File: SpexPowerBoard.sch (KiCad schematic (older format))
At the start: 12 parts

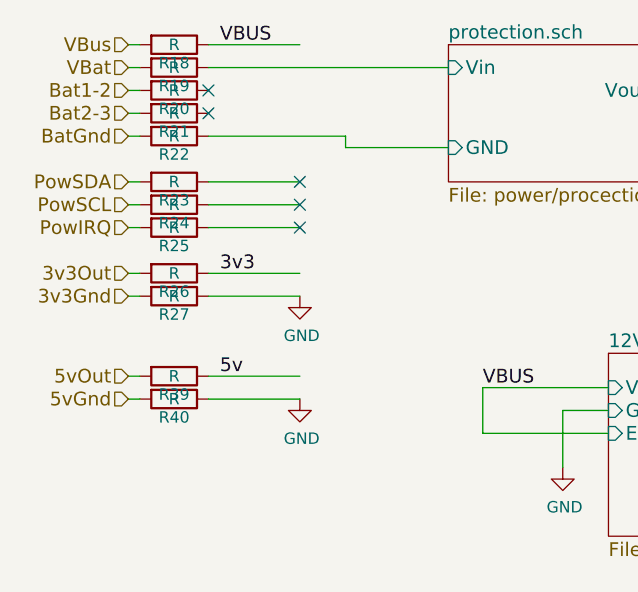
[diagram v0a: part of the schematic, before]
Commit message: Added powerz
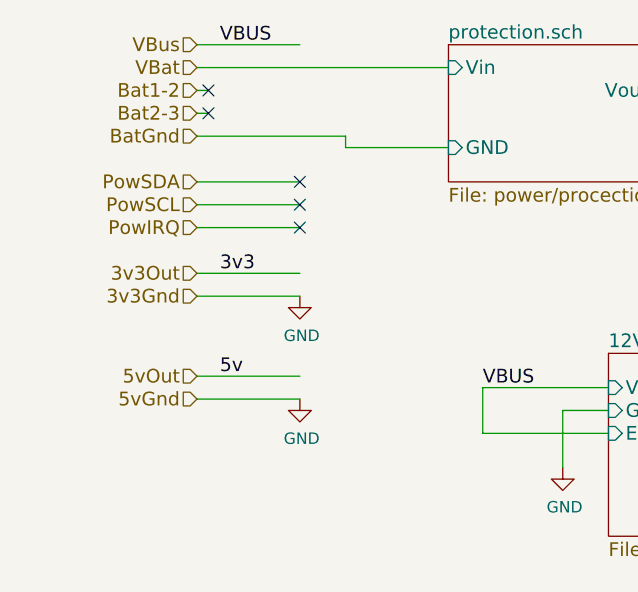
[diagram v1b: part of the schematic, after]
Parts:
- removed R18, R19, R20, R21, R22, R23, R24, R25, R26, R27, R39, R40: R, Resistors_SMD:R_0603, symbol R
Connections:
- wire segments 37 -> 27
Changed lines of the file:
@@
 Comment4 ""
 $EndDescr
-Text HLabel 1950 800  0    60   Input ~ 0
+Text HLabel 2250 800  0    60   Input ~ 0
 VBus
-Text HLabel 1950 900  0    60   Input ~ 0
+Text HLabel 2250 900  0    60   Input ~ 0
 VBat
-Text HLabel 1950 1000 0    60   Input ~ 0
+Text HLabel 2250 1000 0    60   Input ~ 0
 Bat1-2
-Text HLabel 1950 1100 0    60   Input ~ 0
+Text HLabel 2250 1100 0    60   Input ~ 0
 Bat2-3
-Text HLabel 1950 1200 0    60   Input ~ 0
+Text HLabel 2250 1200 0    60   Input ~ 0
 BatGnd
-Text HLabel 1950 1400 0    60   Input ~ 0
+Text HLabel 2250 1400 0    60   Input ~ 0
 PowSDA
-Text HLabel 1950 1500 0    60   Input ~ 0
+Text HLabel 2250 1500 0    60   Input ~ 0
 PowSCL
-Text HLabel 1950 1600 0    60   Input ~ 0
+Text HLabel 2250 1600 0    60   Input ~ 0
 PowIRQ
-Text HLabel 1950 1800 0    60   Input ~ 0
+Text HLabel 2250 1800 0    60   Input ~ 0
 3v3Out
-Text HLabel 1950 1900 0    60   Input ~ 0
+Text HLabel 2250 1900 0    60   Input ~ 0
 3v3Gnd
-$Comp
-L R R18
-U 1 1 56DE6203
-P 2150 800
-F 0 "R18" V 2230 800 50  0000 C CNN
-F 1 "R" V 2150 800 50  0000 C CNN
-F 2 "Resistors_SMD:R_0603" V 2080 800 50  0001 C CNN
-F 3 "" H 2150 800 50  0000 C CNN
-	1    2150 800
-	0    1    1    0
-$EndComp
-$Comp
-L R R19
-U 1 1 56DE621B
-P 2150 900
-F 0 "R19" V 2230 900 50  0000 C CNN
-F 1 "R" V 2150 900 50  0000 C CNN
-F 2 "Resistors_SMD:R_0603" V 2080 900 50  0001 C CNN
-F 3 "" H 2150 900 50  0000 C CNN
-	1    2150 900
-	0    1    1    0
-$EndComp
-$Comp
-L R R20
-U 1 1 56DE6236
-P 2150 1000
-F 0 "R20" V 2230 1000 50  0000 C CNN
-F 1 "R" V 2150 1000 50  0000 C CNN
-F 2 "Resistors_SMD:R_0603" V 2080 1000 50  0001 C CNN
-F 3 "" H 2150 1000 50  0000 C CNN
-	1    2150 1000
-	0    1    1    0
-$EndComp
-$Comp
-L R R21
-U 1 1 56DE6251
-P 2150 1100
-F 0 "R21" V 2230 1100 50  0000 C CNN
-F 1 "R" V 2150 1100 50  0000 C CNN
-F 2 "Resistors_SMD:R_0603" V 2080 1100 50  0001 C CNN
-F 3 "" H 2150 1100 50  0000 C CNN
-	1    2150 1100
-	0    1    1    0
-$EndComp
-$Comp
-L R R22
-U 1 1 56DE626E
-P 2150 1200
-F 0 "R22" V 2230 1200 50  0000 C CNN
-F 1 "R" V 2150 1200 50  0000 C CNN
-F 2 "Resistors_SMD:R_0603" V 2080 1200 50  0001 C CNN
-F 3 "" H 2150 1200 50  0000 C CNN
-	1    2150 1200
-	0    1    1    0
-$EndComp
-$Comp
-L R R23
-U 1 1 56DE6291
-P 2150 1400
-F 0 "R23" V 2230 1400 50  0000 C CNN
-F 1 "R" V 2150 1400 50  0000 C CNN
-F 2 "Resistors_SMD:R_0603" V 2080 1400 50  0001 C CNN
-F 3 "" H 2150 1400 50  0000 C CNN
-	1    2150 1400
-	0    1    1    0
-$EndComp
-$Comp
-L R R24
-U 1 1 56DE62B4
-P 2150 1500
-F 0 "R24" V 2230 1500 50  0000 C CNN
-F 1 "R" V 2150 1500 50  0000 C CNN
-F 2 "Resistors_SMD:R_0603" V 2080 1500 50  0001 C CNN
-F 3 "" H 2150 1500 50  0000 C CNN
-	1    2150 1500
-	0    1    1    0
-$EndComp
-$Comp
-L R R25
-U 1 1 56DE62DB
-P 2150 1600
-F 0 "R25" V 2230 1600 50  0000 C CNN
-F 1 "R" V 2150 1600 50  0000 C CNN
-F 2 "Resistors_SMD:R_0603" V 2080 1600 50  0001 C CNN
-F 3 "" H 2150 1600 50  0000 C CNN
-	1    2150 1600
-	0    1    1    0
-$EndComp
-$Comp
-L R R26
-U 1 1 56DE6304
-P 2150 1800
-F 0 "R26" V 2230 1800 50  0000 C CNN
-F 1 "R" V 2150 1800 50  0000 C CNN
-F 2 "Resistors_SMD:R_0603" V 2080 1800 50  0001 C CNN
-F 3 "" H 2150 1800 50  0000 C CNN
-	1    2150 1800
-	0    1    1    0
-$EndComp
-$Comp
-L R R27
-U 1 1 56DE632D
-P 2150 1900
-F 0 "R27" V 2230 1900 50  0000 C CNN
-F 1 "R" V 2150 1900 50  0000 C CNN
-F 2 "Resistors_SMD:R_0603" V 2080 1900 50  0001 C CNN
-F 3 "" H 2150 1900 50  0000 C CNN
-	1    2150 1900
-	0    1    1    0
-$EndComp
 $Sheet
 S 4050 2150 800  800
@@
 VBUS
 $Comp
-L GND #PWR057
+L GND #PWR058
 U 1 1 56FE58A8
 P 3850 2650
-F 0 "#PWR057" H 3850 2400 50  0001 C CNN
+F 0 "#PWR058" H 3850 2400 50  0001 C CNN
 F 1 "GND" H 3858 2477 50  0000 C CNN
 F 2 "" H 3850 2650 50  0000 C CNN
@@
 $EndComp
 Wire Wire Line
-	1950 800  2000 800
+	2250 800  2700 800
 Wire Wire Line
-	1950 900  2000 900
+	2250 900  3350 900
 Wire Wire Line
-	1950 1000 2000 1000
+	2250 1000 2300 1000
 Wire Wire Line
-	1950 1100 2000 1100
+	2250 1100 2300 1100
 Wire Wire Line
-	1950 1200 2000 1200
+	2250 1200 2900 1200
 Wire Wire Line
-	1950 1400 2000 1400
+	2250 1400 2700 1400
 Wire Wire Line
-	1950 1500 2000 1500
+	2250 1500 2700 1500
 Wire Wire Line
-	1950 1600 2000 1600
+	2250 1600 2700 1600
 Wire Wire Line
-	1950 1800 2000 1800
+	2250 1800 2700 1800
 Wire Wire Line
-	1950 1900 2000 1900
-Wire Wire Line
-	2300 900  3350 900
+	2250 1900 2700 1900
 Wire Wire Line
 	2900 1250 3350 1250
 Wire Wire Line
-	2900 1250 2900 1200
-Wire Wire Line
-	2900 1200 2300 1200
+	2900 1200 2900 1250
 Wire Wire Line
 	4300 1000 4550 1000
@@
 VBUS
 $Comp
-L GND #PWR058
+L GND #PWR059
 U 1 1 56FE6215
 P 3850 4250
-F 0 "#PWR058" H 3850 4000 50  0001 C CNN
+F 0 "#PWR059" H 3850 4000 50  0001 C CNN
 F 1 "GND" H 3858 4077 50  0000 C CNN
 F 2 "" H 3850 4250 50  0000 C CNN
@@
 Text Label 4900 3950 0    60   ~ 0
 5v
-Wire Wire Line
-	2300 1400 2700 1400
-Wire Wire Line
-	2300 1500 2700 1500
-Wire Wire Line
-	2300 1600 2700 1600
-Wire Wire Line
-	2300 1800 2700 1800
-Wire Wire Line
-	2300 1900 2700 1900
 Text Label 2350 1800 0    60   ~ 0
 3v3
 $Comp
-L GND #PWR059
+L GND #PWR060
 U 1 1 56FE74FE
 P 2700 1900
-F 0 "#PWR059" H 2700 1650 50  0001 C CNN
+F 0 "#PWR060" H 2700 1650 50  0001 C CNN
 F 1 "GND" H 2708 1727 50  0000 C CNN
 F 2 "" H 2700 1900 50  0000 C CNN
@@
 NoConn ~ 2300 1000
 NoConn ~ 2300 1100
-Wire Wire Line
-	2300 800  2700 800
 Text Label 2350 800  0    60   ~ 0
 VBUS
-Text HLabel 1950 2250 0    60   Input ~ 0
+Text HLabel 2250 2250 0    60   Input ~ 0
 5vOut
-Text HLabel 1950 2350 0    60   Input ~ 0
+Text HLabel 2250 2350 0    60   Input ~ 0
 5vGnd
-$Comp
-L R R39
-U 1 1 56FE7B52
-P 2150 2250
-F 0 "R39" V 2230 2250 50  0000 C CNN
-F 1 "R" V 2150 2250 50  0000 C CNN
-F 2 "Resistors_SMD:R_0603" V 2080 2250 50  0001 C CNN
-F 3 "" H 2150 2250 50  0000 C CNN
-	1    2150 2250
-	0    1    1    0
-$EndComp
-$Comp
-L R R40
-U 1 1 56FE7B58
-P 2150 2350
-F 0 "R40" V 2230 2350 50  0000 C CNN
-F 1 "R" V 2150 2350 50  0000 C CNN
-F 2 "Resistors_SMD:R_0603" V 2080 2350 50  0001 C CNN
-F 3 "" H 2150 2350 50  0000 C CNN
-	1    2150 2350
-	0    1    1    0
-$EndComp
 Wire Wire Line
-	1950 2250 2000 2250
+	2250 2250 2700 2250
 Wire Wire Line
-	1950 2350 2000 2350
-Wire Wire Line
-	2300 2250 2700 2250
-Wire Wire Line
-	2300 2350 2700 2350
+	2250 2350 2700 2350
 Text Label 2350 2250 0    60   ~ 0
 5v
 $Comp
-L GND #PWR060
+L GND #PWR061
 U 1 1 56FE7B63
 P 2700 2350
-F 0 "#PWR060" H 2700 2100 50  0001 C CNN
+F 0 "#PWR061" H 2700 2100 50  0001 C CNN
 F 1 "GND" H 2708 2177 50  0000 C CNN
 F 2 "" H 2700 2350 50  0000 C CNN

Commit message: completed first revision of the board.
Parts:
- added P13: CONN_01X02, SPEX_Parts:ultraFitCONN_2, symbol CONN_01X02
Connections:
- wire segments 27 -> 30
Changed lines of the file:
@@
 3v3Gnd
 $Sheet
-S 4050 2150 800  800
+S 5600 800  800  800
 U 56FE3A4E
 F0 "12Vto3v3.sch" 60
 F1 "power/12Vto3v3.sch" 60
-F2 "Vin" I L 4050 2300 60
-F3 "Gnd" I L 4050 2400 60
-F4 "En" I L 4050 2500 60
-F5 "Vout" I R 4850 2300 60
+F2 "Vin" I L 5600 950 60
+F3 "Gnd" I L 5600 1050 60
+F4 "En" I L 5600 1150 60
+F5 "Vout" I R 6400 950 60
 $EndSheet
 $Sheet
@@
 Text Label 4300 1000 0    60   ~ 0
 VBUS
-Text Label 3500 2300 0    60   ~ 0
+Text Label 5050 950  0    60   ~ 0
 VBUS
 $Comp
 L GND #PWR058
 U 1 1 56FE58A8
-P 3850 2650
-F 0 "#PWR058" H 3850 2400 50  0001 C CNN
-F 1 "GND" H 3858 2477 50  0000 C CNN
-F 2 "" H 3850 2650 50  0000 C CNN
-F 3 "" H 3850 2650 50  0000 C CNN
-	1    3850 2650
+P 5400 1300
+F 0 "#PWR058" H 5400 1050 50  0001 C CNN
+F 1 "GND" H 5408 1127 50  0000 C CNN
+F 2 "" H 5400 1300 50  0000 C CNN
+F 3 "" H 5400 1300 50  0000 C CNN
+	1    5400 1300
 	1    0    0    -1
 $EndComp
@@
 	4300 1000 4550 1000
 Wire Wire Line
-	4050 2300 3500 2300
+	5600 950  5050 950
 Wire Wire Line
-	4050 2500 3500 2500
+	5600 1150 5050 1150
 Wire Wire Line
-	3500 2500 3500 2300
+	5050 1150 5050 950
 Wire Wire Line
-	3850 2400 4050 2400
+	5400 1050 5600 1050
 Wire Wire Line
-	3850 2400 3850 2650
+	5400 1050 5400 1300
 Wire Wire Line
-	4850 2300 5200 2300
-Text Label 4900 2300 0    60   ~ 0
+	6400 950  6750 950
+Text Label 6450 950  0    60   ~ 0
 3v3
-Text Label 3500 3900 0    60   ~ 0
+Text Label 7350 1100 0    60   ~ 0
 VBUS
 $Comp
 L GND #PWR059
 U 1 1 56FE6215
-P 3850 4250
-F 0 "#PWR059" H 3850 4000 50  0001 C CNN
-F 1 "GND" H 3858 4077 50  0000 C CNN
-F 2 "" H 3850 4250 50  0000 C CNN
-F 3 "" H 3850 4250 50  0000 C CNN
-	1    3850 4250
+P 7700 1450
+F 0 "#PWR059" H 7700 1200 50  0001 C CNN
+F 1 "GND" H 7708 1277 50  0000 C CNN
+F 2 "" H 7700 1450 50  0000 C CNN
+F 3 "" H 7700 1450 50  0000 C CNN
+	1    7700 1450
 	1    0    0    -1
 $EndComp
 Wire Wire Line
-	4050 3900 3500 3900
+	7900 1100 7350 1100
 Wire Wire Line
-	4050 4100 3500 4100
+	7900 1300 7350 1300
 Wire Wire Line
-	3500 4100 3500 3900
+	7350 1300 7350 1100
 Wire Wire Line
-	3850 4000 4050 4000
+	7700 1200 7900 1200
 Wire Wire Line
-	3850 4000 3850 4250
+	7700 1200 7700 1450
 $Sheet
-S 4050 3600 800  750
+S 7900 800  800  750
 U 56FE62EA
 F0 "12Vto5V.sch" 60
 F1 "power/12Vto5V.sch" 60
-F2 "Vin" I L 4050 3900 60
-F3 "Gnd" I L 4050 4000 60
-F4 "En" I L 4050 4100 60
-F5 "Vout" I R 4850 3950 60
+F2 "Vin" I L 7900 1100 60
+F3 "Gnd" I L 7900 1200 60
+F4 "En" I L 7900 1300 60
+F5 "Vout" I R 8700 1150 60
 $EndSheet
 Wire Wire Line
-	4850 3950 5150 3950
-Text Label 4900 3950 0    60   ~ 0
+	8700 1150 9000 1150
+Text Label 8750 1150 0    60   ~ 0
 5v
 Text Label 2350 1800 0    60   ~ 0
@@
 	1    0    0    -1
 $EndComp
+$Comp
+L CONN_01X02 P13
+U 1 1 57082C77
+P 850 1000
+F 0 "P13" H 850 1150 50  0000 C CNN
+F 1 "CONN_01X02" V 950 1000 50  0000 C CNN
+F 2 "SPEX_Parts:ultraFitCONN_2" H 850 1000 50  0001 C CNN
+F 3 "" H 850 1000 50  0000 C CNN
+	1    850  1000
+	-1   0    0    1
+$EndComp
+$Comp
+L GND #PWR062
+U 1 1 57082F19
+P 1100 1100
+F 0 "#PWR062" H 1100 850 50  0001 C CNN
+F 1 "GND" H 1108 927 50  0000 C CNN
+F 2 "" H 1100 1100 50  0000 C CNN
+F 3 "" H 1100 1100 50  0000 C CNN
+	1    1100 1100
+	1    0    0    -1
+$EndComp
+Wire Wire Line
+	1050 1050 1100 1050
+Wire Wire Line
+	1100 1050 1100 1100
+Text HLabel 1150 950  2    60   Input ~ 0
+VBat
+Wire Wire Line
+	1150 950  1050 950
 $EndSCHEMATC

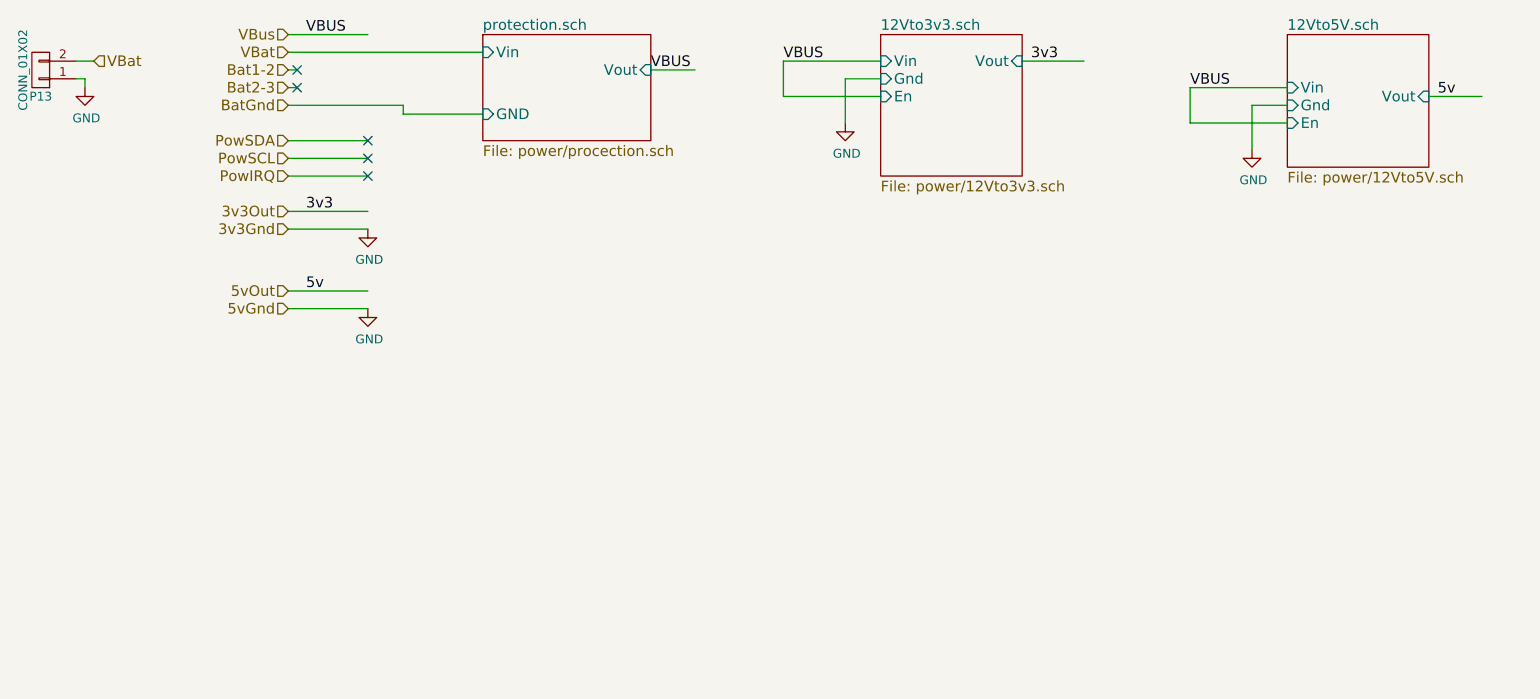
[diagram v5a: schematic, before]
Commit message: rev 2 of hab board in progress
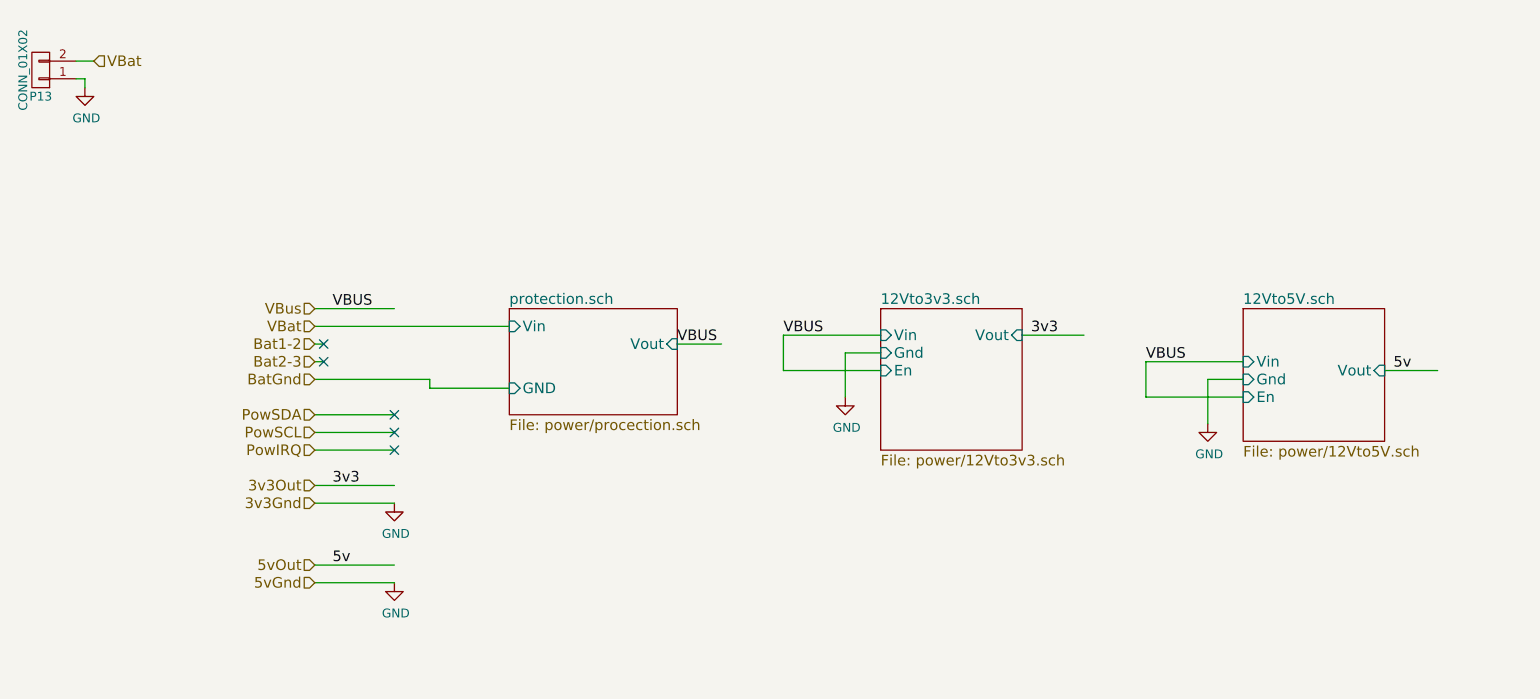
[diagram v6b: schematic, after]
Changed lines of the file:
@@
 Comment4 ""
 $EndDescr
-Text HLabel 2250 800  0    60   Input ~ 0
+Text HLabel 2400 2350 0    60   Input ~ 0
 VBus
-Text HLabel 2250 900  0    60   Input ~ 0
+Text HLabel 2400 2450 0    60   Input ~ 0
 VBat
-Text HLabel 2250 1000 0    60   Input ~ 0
+Text HLabel 2400 2550 0    60   Input ~ 0
 Bat1-2
-Text HLabel 2250 1100 0    60   Input ~ 0
+Text HLabel 2400 2650 0    60   Input ~ 0
 Bat2-3
-Text HLabel 2250 1200 0    60   Input ~ 0
+Text HLabel 2400 2750 0    60   Input ~ 0
 BatGnd
-Text HLabel 2250 1400 0    60   Input ~ 0
+Text HLabel 2400 2950 0    60   Input ~ 0
 PowSDA
-Text HLabel 2250 1500 0    60   Input ~ 0
+Text HLabel 2400 3050 0    60   Input ~ 0
 PowSCL
-Text HLabel 2250 1600 0    60   Input ~ 0
+Text HLabel 2400 3150 0    60   Input ~ 0
 PowIRQ
-Text HLabel 2250 1800 0    60   Input ~ 0
+Text HLabel 2400 3350 0    60   Input ~ 0
 3v3Out
-Text HLabel 2250 1900 0    60   Input ~ 0
+Text HLabel 2400 3450 0    60   Input ~ 0
 3v3Gnd
 $Sheet
-S 5600 800  800  800
+S 5600 2350 800  800
 U 56FE3A4E
 F0 "12Vto3v3.sch" 60
 F1 "power/12Vto3v3.sch" 60
-F2 "Vin" I L 5600 950 60
-F3 "Gnd" I L 5600 1050 60
-F4 "En" I L 5600 1150 60
-F5 "Vout" I R 6400 950 60
+F2 "Vin" I L 5600 2500 60
+F3 "Gnd" I L 5600 2600 60
+F4 "En" I L 5600 2700 60
+F5 "Vout" I R 6400 2500 60
 $EndSheet
 $Sheet
-S 3350 800  950  600
+S 3500 2350 950  600
 U 56FE3DDD
 F0 "protection.sch" 60
 F1 "power/procection.sch" 60
-F2 "GND" I L 3350 1250 60
-F3 "Vin" I L 3350 900 60
-F4 "Vout" I R 4300 1000 60
+F2 "GND" I L 3500 2800 60
+F3 "Vin" I L 3500 2450 60
+F4 "Vout" I R 4450 2550 60
 $EndSheet
-Text Label 4300 1000 0    60   ~ 0
+Text Label 4450 2550 0    60   ~ 0
 VBUS
-Text Label 5050 950  0    60   ~ 0
+Text Label 5050 2500 0    60   ~ 0
 VBUS
 $Comp
-L GND #PWR058
+L GND #PWR059
 U 1 1 56FE58A8
-P 5400 1300
-F 0 "#PWR058" H 5400 1050 50  0001 C CNN
-F 1 "GND" H 5408 1127 50  0000 C CNN
-F 2 "" H 5400 1300 50  0000 C CNN
-F 3 "" H 5400 1300 50  0000 C CNN
-	1    5400 1300
+P 5400 2850
+F 0 "#PWR059" H 5400 2600 50  0001 C CNN
+F 1 "GND" H 5408 2677 50  0000 C CNN
+F 2 "" H 5400 2850 50  0000 C CNN
+F 3 "" H 5400 2850 50  0000 C CNN
+	1    5400 2850
 	1    0    0    -1
 $EndComp
 Wire Wire Line
-	2250 800  2700 800
+	2400 2350 2850 2350
 Wire Wire Line
-	2250 900  3350 900
+	2400 2450 3500 2450
 Wire Wire Line
-	2250 1000 2300 1000
+	2400 2550 2450 2550
 Wire Wire Line
-	2250 1100 2300 1100
+	2400 2650 2450 2650
 Wire Wire Line
-	2250 1200 2900 1200
+	2400 2750 3050 2750
 Wire Wire Line
-	2250 1400 2700 1400
+	2400 2950 2850 2950
 Wire Wire Line
-	2250 1500 2700 1500
+	2400 3050 2850 3050
 Wire Wire Line
-	2250 1600 2700 1600
+	2400 3150 2850 3150
 Wire Wire Line
-	2250 1800 2700 1800
+	2400 3350 2850 3350
 Wire Wire Line
-	2250 1900 2700 1900
+	2400 3450 2850 3450
 Wire Wire Line
-	2900 1250 3350 1250
+	3050 2800 3500 2800
 Wire Wire Line
-	2900 1200 2900 1250
+	3050 2750 3050 2800
 Wire Wire Line
-	4300 1000 4550 1000
+	4450 2550 4700 2550
 Wire Wire Line
-	5600 950  5050 950
+	5600 2500 5050 2500
 Wire Wire Line
-	5600 1150 5050 1150
+	5600 2700 5050 2700
 Wire Wire Line
-	5050 1150 5050 950
+	5050 2700 5050 2500
 Wire Wire Line
-	5400 1050 5600 1050
+	5400 2600 5600 2600
 Wire Wire Line
-	5400 1050 5400 1300
+	5400 2600 5400 2850
 Wire Wire Line
-	6400 950  6750 950
-Text Label 6450 950  0    60   ~ 0
+	6400 2500 6750 2500
+Text Label 6450 2500 0    60   ~ 0
 3v3
-Text Label 7350 1100 0    60   ~ 0
+Text Label 7100 2650 0    60   ~ 0
 VBUS
 $Comp
-L GND #PWR059
+L GND #PWR060
 U 1 1 56FE6215
-P 7700 1450
-F 0 "#PWR059" H 7700 1200 50  0001 C CNN
-F 1 "GND" H 7708 1277 50  0000 C CNN
-F 2 "" H 7700 1450 50  0000 C CNN
-F 3 "" H 7700 1450 50  0000 C CNN
-	1    7700 1450
+P 7450 3000
+F 0 "#PWR060" H 7450 2750 50  0001 C CNN
+F 1 "GND" H 7458 2827 50  0000 C CNN
+F 2 "" H 7450 3000 50  0000 C CNN
+F 3 "" H 7450 3000 50  0000 C CNN
+	1    7450 3000
 	1    0    0    -1
 $EndComp
 Wire Wire Line
-	7900 1100 7350 1100
+	7650 2650 7100 2650
 Wire Wire Line
-	7900 1300 7350 1300
+	7650 2850 7100 2850
 Wire Wire Line
-	7350 1300 7350 1100
+	7100 2850 7100 2650
 Wire Wire Line
-	7700 1200 7900 1200
+	7450 2750 7650 2750
 Wire Wire Line
-	7700 1200 7700 1450
+	7450 2750 7450 3000
 $Sheet
-S 7900 800  800  750
+S 7650 2350 800  750
 U 56FE62EA
 F0 "12Vto5V.sch" 60
 F1 "power/12Vto5V.sch" 60
-F2 "Vin" I L 7900 1100 60
-F3 "Gnd" I L 7900 1200 60
-F4 "En" I L 7900 1300 60
-F5 "Vout" I R 8700 1150 60
+F2 "Vin" I L 7650 2650 60
+F3 "Gnd" I L 7650 2750 60
+F4 "En" I L 7650 2850 60
+F5 "Vout" I R 8450 2700 60
 $EndSheet
 Wire Wire Line
-	8700 1150 9000 1150
-Text Label 8750 1150 0    60   ~ 0
+	8450 2700 8750 2700
+Text Label 8500 2700 0    60   ~ 0
 5v
-Text Label 2350 1800 0    60   ~ 0
+Text Label 2500 3350 0    60   ~ 0
 3v3
 $Comp
-L GND #PWR060
+L GND #PWR061
 U 1 1 56FE74FE
-P 2700 1900
-F 0 "#PWR060" H 2700 1650 50  0001 C CNN
-F 1 "GND" H 2708 1727 50  0000 C CNN
-F 2 "" H 2700 1900 50  0000 C CNN
-F 3 "" H 2700 1900 50  0000 C CNN
-	1    2700 1900
+P 2850 3450
+F 0 "#PWR061" H 2850 3200 50  0001 C CNN
+F 1 "GND" H 2858 3277 50  0000 C CNN
+F 2 "" H 2850 3450 50  0000 C CNN
+F 3 "" H 2850 3450 50  0000 C CNN
+	1    2850 3450
 	1    0    0    -1
 $EndComp
-NoConn ~ 2700 1400
-NoConn ~ 2700 1500
-NoConn ~ 2700 1600
-NoConn ~ 2300 1000
-NoConn ~ 2300 1100
-Text Label 2350 800  0    60   ~ 0
+NoConn ~ 2850 2950
+NoConn ~ 2850 3050
+NoConn ~ 2850 3150
+NoConn ~ 2450 2550
+NoConn ~ 2450 2650
+Text Label 2500 2350 0    60   ~ 0
 VBUS
-Text HLabel 2250 2250 0    60   Input ~ 0
+Text HLabel 2400 3800 0    60   Input ~ 0
 5vOut
-Text HLabel 2250 2350 0    60   Input ~ 0
+Text HLabel 2400 3900 0    60   Input ~ 0
 5vGnd
 Wire Wire Line
-	2250 2250 2700 2250
+	2400 3800 2850 3800
 Wire Wire Line
-	2250 2350 2700 2350
-Text Label 2350 2250 0    60   ~ 0
+	2400 3900 2850 3900
+Text Label 2500 3800 0    60   ~ 0
 5v
 $Comp
-L GND #PWR061
+L GND #PWR062
 U 1 1 56FE7B63
-P 2700 2350
-F 0 "#PWR061" H 2700 2100 50  0001 C CNN
-F 1 "GND" H 2708 2177 50  0000 C CNN
-F 2 "" H 2700 2350 50  0000 C CNN
-F 3 "" H 2700 2350 50  0000 C CNN
-	1    2700 2350
+P 2850 3900
+F 0 "#PWR062" H 2850 3650 50  0001 C CNN
+F 1 "GND" H 2858 3727 50  0000 C CNN
+F 2 "" H 2850 3900 50  0000 C CNN
+F 3 "" H 2850 3900 50  0000 C CNN
+	1    2850 3900
 	1    0    0    -1
 $EndComp
@@
 $EndComp
 $Comp
-L GND #PWR062
+L GND #PWR063
 U 1 1 57082F19
 P 1100 1100
-F 0 "#PWR062" H 1100 850 50  0001 C CNN
+F 0 "#PWR063" H 1100 850 50  0001 C CNN
 F 1 "GND" H 1108 927 50  0000 C CNN
 F 2 "" H 1100 1100 50  0000 C CNN
